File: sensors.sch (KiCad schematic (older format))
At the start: 79 parts, among them U2 BQ32000, X1 32768Hz

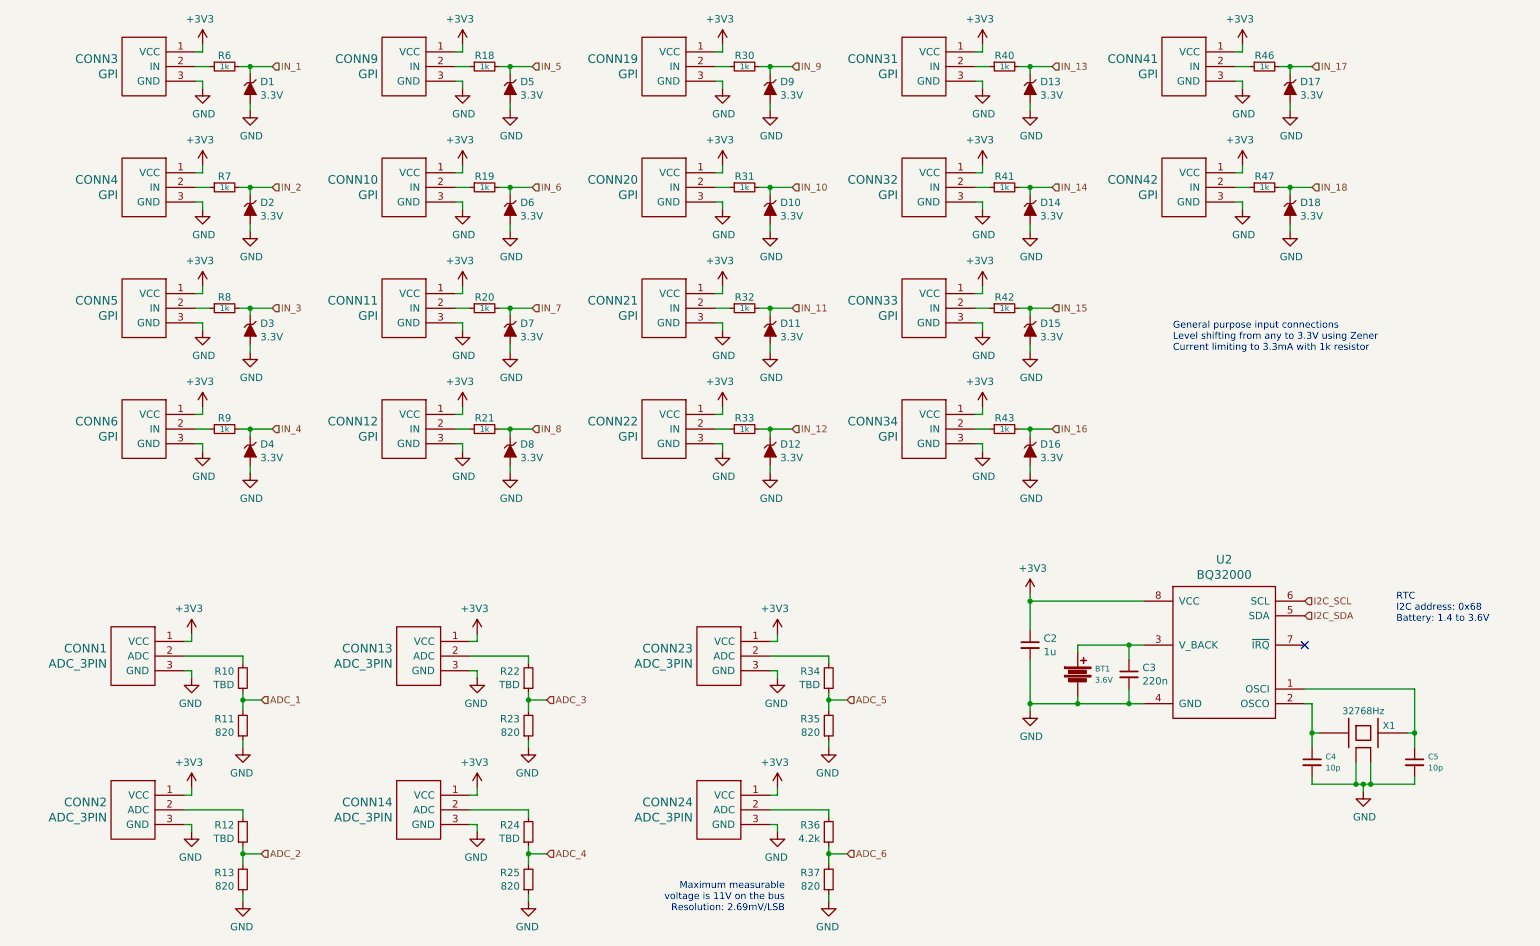
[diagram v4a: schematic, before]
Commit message: Add decoupling capacitors at ADC inputs
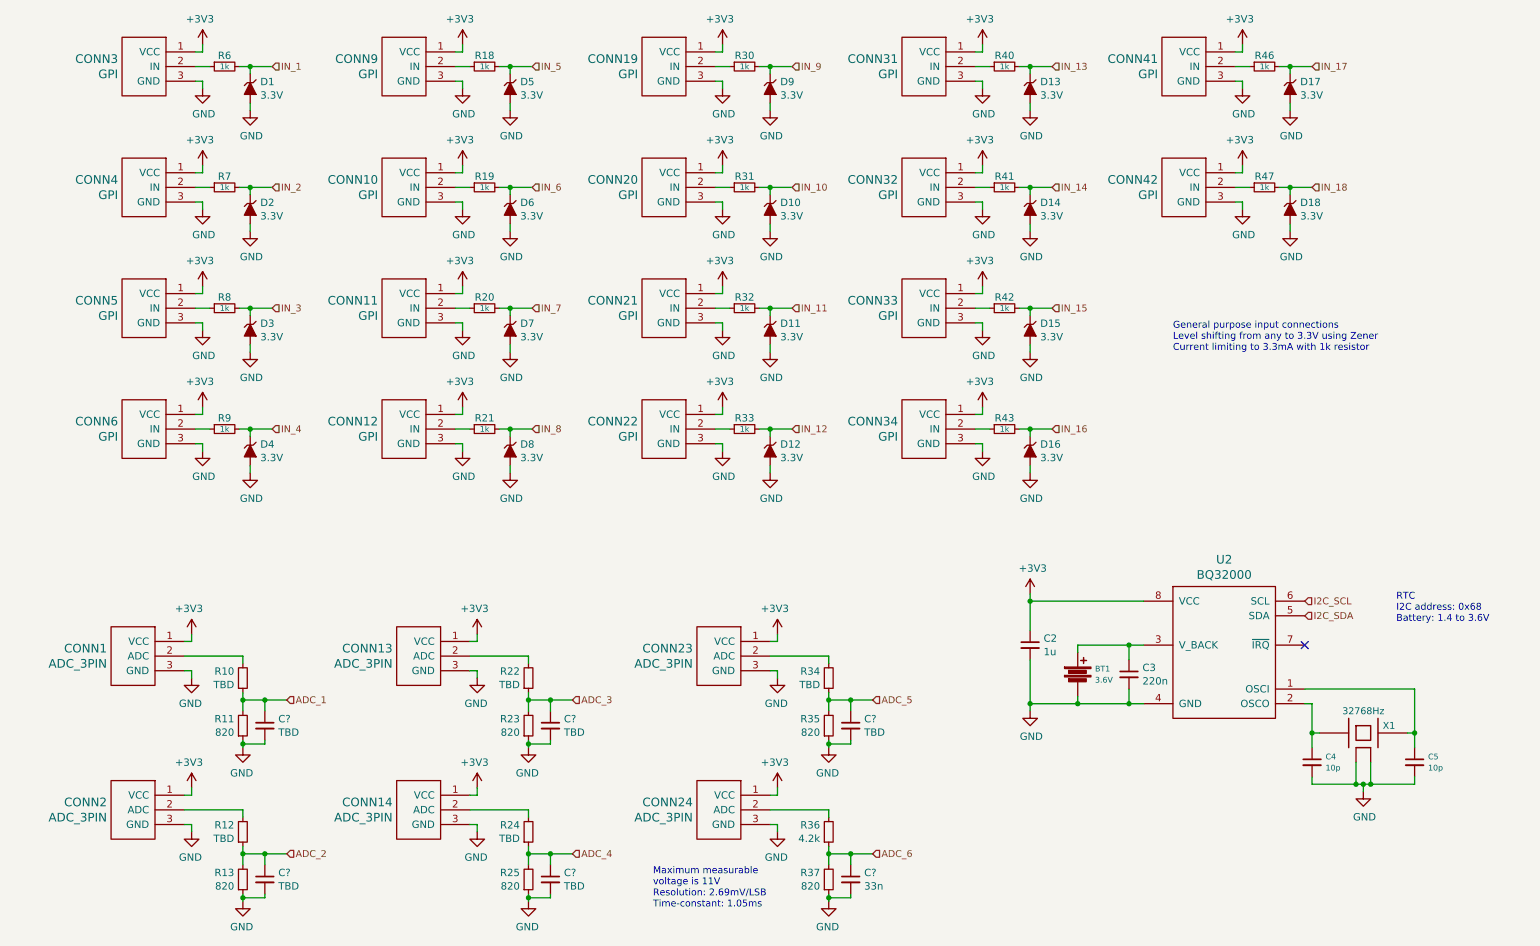
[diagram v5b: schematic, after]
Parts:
- added C? (x5): TBD, symbol C_Small
- added C?: 33n, symbol C_Small
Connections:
- net ADC_1: now also C?.1
- net ADC_2: now also C?.1
- net ADC_3: now also C?.1
- net ADC_4: now also C?.1
- net ADC_5: now also C?.1
- net ADC_6: now also C?.1
- net GND: now also C?.2, C?.2, C?.2, C?.2, C?.2, C?.2
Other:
- note added: "Maximum measurable\nvoltage is 11V\nResolution: 2.69mV/LSB\nTime-constant: 1.05ms"
- note removed: "Maximum measurable \nvoltage is 11V on the bus\nResolution: 2.69mV/LSB"

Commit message: Correct digital outputs as we want to drive loads (LEDs)
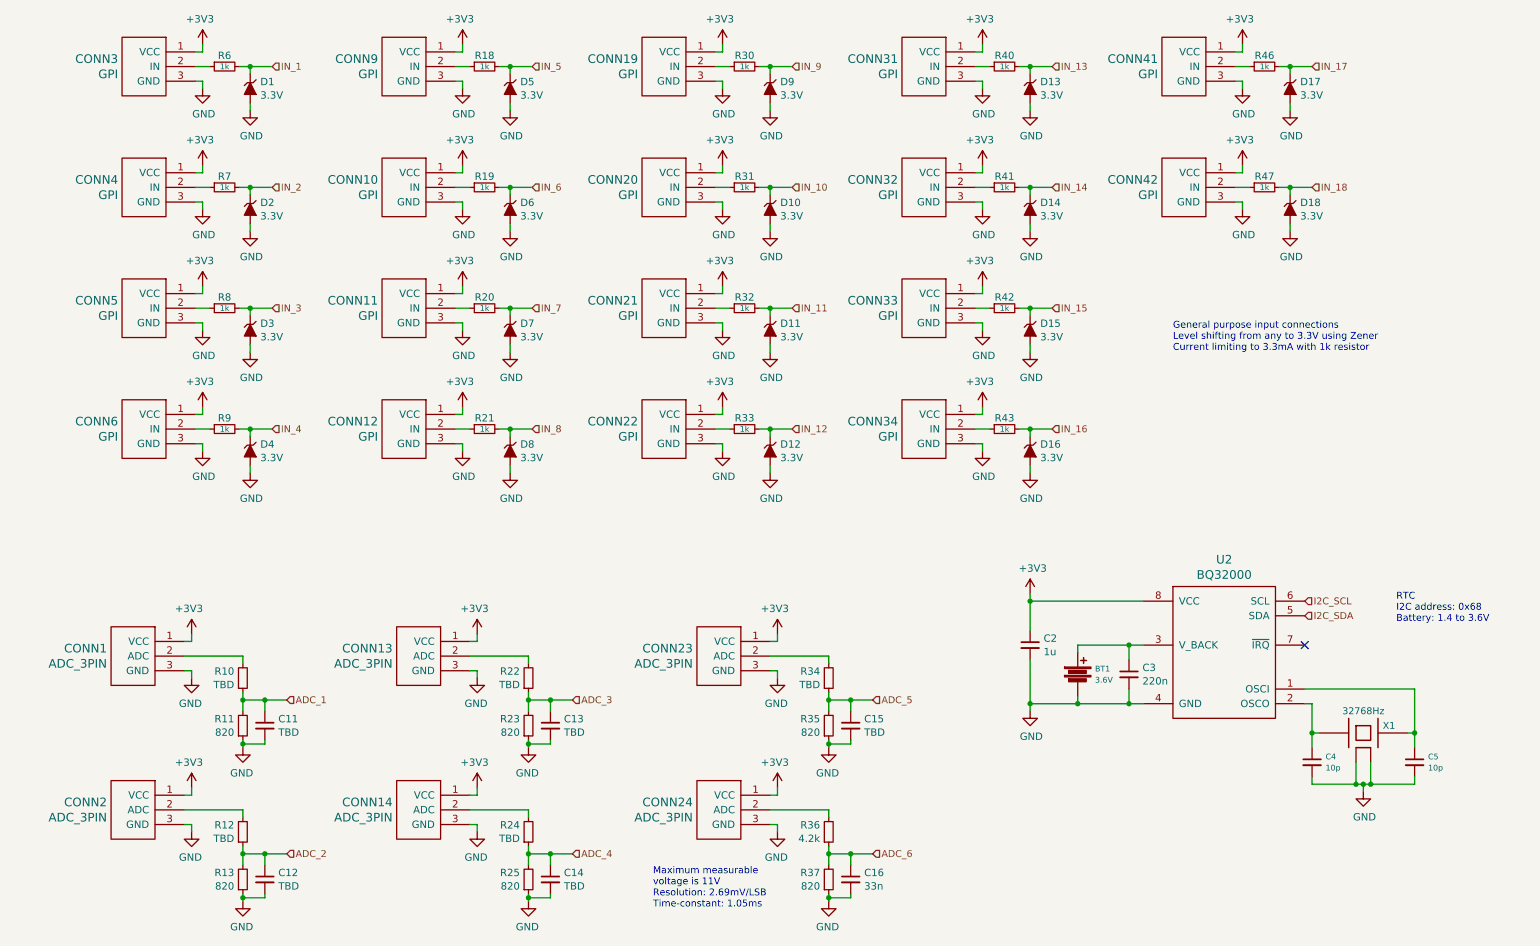
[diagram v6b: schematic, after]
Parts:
- gave numbers to parts that had none: 6

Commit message: Wire inputs from switches correctly
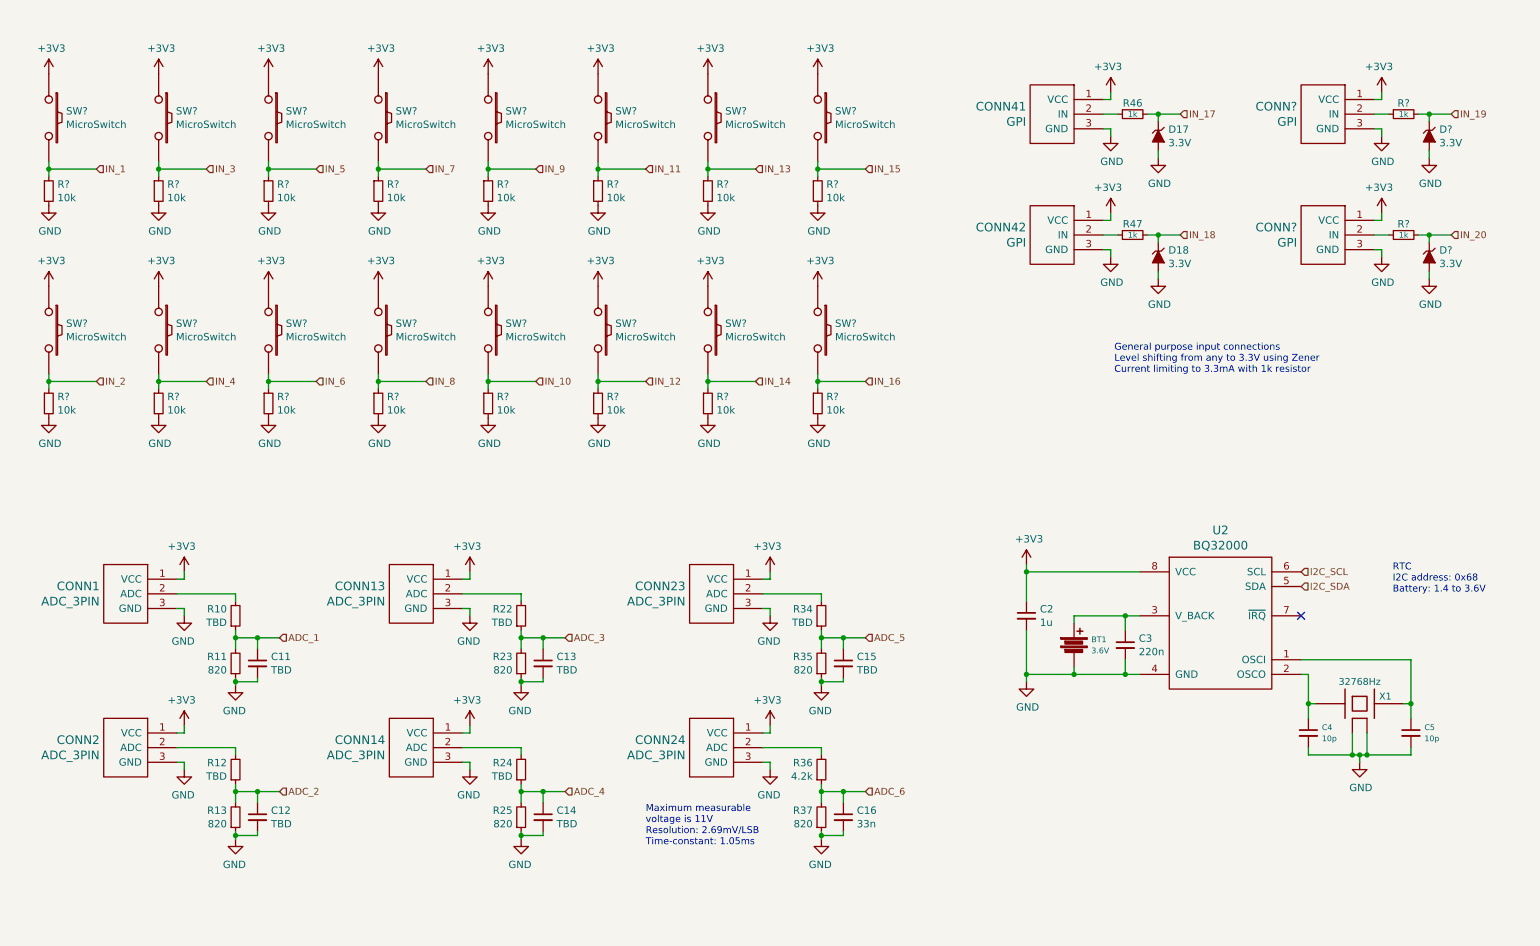
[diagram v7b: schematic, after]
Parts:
- removed CONN10, CONN11, CONN12, CONN19, CONN20, CONN21, CONN22, CONN3, CONN31, CONN32, CONN33, CONN34, CONN4, CONN5, CONN6, CONN9: GPI, symbol GPI
- removed D1, D10, D11, D12, D13, D14, D15, D16, D2, D3, D4, D5, D6, D7, D8, D9: 3.3V, symbol ZENERsmall
- removed R18, R19, R20, R21, R30, R31, R32, R33, R40, R41, R42, R43, R6, R7, R8, R9: 1k, symbol R_Small
- added CONN? (x2): GPI, symbol GPI
- added D? (x2): 3.3V, symbol ZENERsmall
- added R? (x16): 10k, symbol R_Small
- added R? (x2): 1k, symbol R_Small
- added SW? (x16): MicroSwitch, symbol SW_PUSH
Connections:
- net +3V3: now also CONN?.1 (VCC), CONN?.1 (VCC), SW?.1, SW?.1, SW?.1, SW?.1, SW?.1, SW?.1, SW?.1, SW?.1, SW?.1, SW?.1, SW?.1, SW?.1, SW?.1, SW?.1, SW?.1, SW?.1
- net GND: now also CONN?.3 (GND), CONN?.3 (GND), D?.2 (A), D?.2 (A), R?.2, R?.2, R?.2, R?.2, R?.2, R?.2, R?.2, R?.2, R?.2, R?.2, R?.2, R?.2, R?.2, R?.2, R?.2, R?.2
- net IN_1: now also R?.1, SW?.2
- net IN_10: now also R?.1, SW?.2
- net IN_11: now also R?.1, SW?.2
- net IN_12: now also R?.1, SW?.2
- net IN_13: now also R?.1, SW?.2
- net IN_14: now also R?.1, SW?.2
- net IN_15: now also R?.1, SW?.2
- net IN_16: now also R?.1, SW?.2
- net IN_2: now also R?.1, SW?.2
- net IN_3: now also R?.1, SW?.2
- net IN_4: now also R?.1, SW?.2
- net IN_5: now also R?.1, SW?.2
- net IN_6: now also R?.1, SW?.2
- net IN_7: now also R?.1, SW?.2
- net IN_8: now also R?.1, SW?.2
- net IN_9: now also R?.1, SW?.2
- new net: CONN?.2 (IN), R?.1 (x2)
- new net IN_19: D?.1 (K), R?.2
- new net IN_20: D?.1 (K), R?.2
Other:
- moved on the sheet: BT1, C11, C12, C13, C14, C15, C16, C2, C3, C4, C5, CONN1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

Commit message: Fix small details & replot pdf
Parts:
- removed CONN1, CONN13, CONN14, CONN2, CONN23, CONN24: ADC_3PIN, symbol ADC_3PIN
- added CONN10, CONN11, CONN12, CONN7, CONN8, CONN9: ADC_2PIN, symbol ADC_2PIN
- gave numbers to parts that had none: 38
- renumbered C14 to C10, C15 to C11, C16 to C12, C2 to C13, C3 to C14, C4 to C15, C5 to C16, C11 to C7, C12 to C8, C13 to C9, CONN41 to CONN13, CONN42 to CONN14, D17 to D2, D18 to D3, R10 to R15, R11 to R16, R12 to R17, R13 to R18, R22 to R25, R23 to R26, R24 to R27, R25 to R28, R34 to R35, R35 to R36, R36 to R37, R37 to R38, R46 to R39, R47 to R40, U2 to U5, X1 to X2
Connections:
- net GND: now also CONN10.2 (GND), CONN11.2 (GND), CONN12.2 (GND), CONN7.2 (GND), CONN8.2 (GND), CONN9.2 (GND)
- net at R15.2: now also CONN7.1 (ADC)
- net at R17.2: now also CONN8.1 (ADC)
- net at R25.2: now also CONN9.1 (ADC)
- net at R27.2: now also CONN10.1 (ADC)
- net at R35.2: now also CONN11.1 (ADC)
- net at R37.2: now also CONN12.1 (ADC)
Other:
- note added: "Laser telemeter IFM input\nMaximum measurable\nvoltage is 11V\nResolution: 2.69mV/LSB\nTime-constant: 1.05ms"
- note removed: "Maximum measurable\nvoltage is 11V\nResolution: 2.69mV/LSB\nTime-constant: 1.05ms"
- moved on the sheet: C7, C8, R15, R16, R17, R18
